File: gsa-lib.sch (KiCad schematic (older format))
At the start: 56 parts

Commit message: Update to support KiCad v5
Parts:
- BR?: symbol BRIDGE -> gsa:BRIDGE
- C?: symbol CAP -> gsa:CAP
- C?: symbol CAP-P -> gsa:CAP-P
- D?: symbol DIODE -> gsa:DIODE
- F?: symbol FUSE -> gsa:FUSE
- GND?: symbol EARTH -> gsa:EARTH
- GND?: symbol GND -> gsa:GND
- H?: symbol HOLE -> gsa:HOLE
- J?: symbol CONN-1 -> gsa:CONN-1
- J?: symbol CONN-2 -> gsa:CONN-2
- J?: symbol CONN-3 -> gsa:CONN-3
- J?: symbol CONN-4 -> gsa:CONN-4
- J?: symbol CONN-5 -> gsa:CONN-5
- LED: symbol LED -> gsa:LED
- Q?: symbol N-JFET -> gsa:N-JFET
- Q?: symbol NMOS-D -> gsa:NMOS-D
- Q?: symbol NMOS-E -> gsa:NMOS-E
- Q?: symbol NPN -> gsa:NPN
- Q?: symbol P-JFET -> gsa:P-JFET
- Q?: symbol PMOS-D -> gsa:PMOS-D
- Q?: symbol PMOS-E -> gsa:PMOS-E
- Q?: symbol PNP -> gsa:PNP
- R?: symbol RES -> gsa:RES
- R?: symbol REZ -> gsa:REZ
- RL?: symbol RELAY-DPDT -> gsa:RELAY-DPDT
- RL?: symbol RELAY-SPDT -> gsa:RELAY-SPDT
- SW?: symbol DPDT -> gsa:DPDT
- SW?: symbol SP-PUSH -> gsa:SP-PUSH
- SW?: symbol SP2T -> gsa:SP2T
- SW?: symbol SP3T -> gsa:SP3T
- SW?: symbol SPDT -> gsa:SPDT
- SW?: symbol SPST -> gsa:SPST
- SW?: symbol DPST -> gsa:DPST
- TX?: symbol XFRMR -> gsa:XFRMR
- TX?: symbol XFRMR-C -> gsa:XFRMR-C
- TX?: symbol XFRMR-D -> gsa:XFRMR-D
- U?: symbol 4017 -> gsa:4017
- U?: symbol 4066 -> gsa:4066
- U?: symbol 741 -> gsa:741
- U?: symbol LM1875 -> gsa:LM1875
- U?: symbol LM1876 -> gsa:LM1876
- U?: symbol LM317 -> gsa:LM317
- U?: symbol LM386 -> gsa:LM386
- U?: symbol LM377 -> gsa:LM377
- U?: symbol LM78XX -> gsa:LM78XX
- U?: symbol LM79XX -> gsa:LM79XX
- U?: symbol NE555 -> gsa:NE555
- U?: symbol OPAMP -> gsa:OPAMP
- U?: symbol TDA2009 -> gsa:TDA2009
- U?: symbol 40106 -> gsa:40106
- U?: symbol 4093 -> gsa:4093
- V?: symbol POWER -> gsa:POWER
- VR?: symbol POT -> gsa:POT
- VR?: symbol VR -> gsa:VR
- X?: symbol LINK -> gsa:LINK
- ZD?: symbol ZENER -> gsa:ZENER
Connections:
- net V+: no longer names the net of V?.1 (V+)
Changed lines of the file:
@@
-EESchema Schematic File Version 2
-LIBS:gsa
-EELAYER 25 0
+EESchema Schematic File Version 4
+LIBS:gsa-lib-cache
+EELAYER 29 0
 EELAYER END
 $Descr A4 11693 8268
@@
 Sheet 1 1
 Title "GSA Schematic Library"
-Date "January 2018"
-Rev "1.0.0"
+Date "January 2019"
+Rev "1.0.1"
 Comp "Gemstone Amplification"
-Comment1 "© Tim Baldwin 2016,2018"
+Comment1 "© Tim Baldwin 2016,2019"
 Comment2 ""
 Comment3 ""
@@
 $EndDescr
 $Comp
-L 4017 U?
+L gsa:4017 U?
 U 1 1 5A8F3386
 P 6700 1650
@@
 $EndComp
 $Comp
-L 4066 U?
+L gsa:4066 U?
 U 1 1 5A8F340F
 P 7350 1650
@@
 $EndComp
 $Comp
-L 741 U?
+L gsa:741 U?
 U 1 1 5A8F34D3
 P 8750 2000
@@
 $EndComp
 $Comp
-L CAP C?
+L gsa:CAP C?
 U 1 1 5A8F35EB
 P 2300 1850
@@
 $EndComp
 $Comp
-L CAP-P C?
+L gsa:CAP-P C?
 U 1 1 5A8F364A
 P 2650 1850
@@
 $EndComp
 $Comp
-L CONN-1 J?
+L gsa:CONN-1 J?
 U 1 1 5A8F36D3
 P 4200 1000
@@
 $EndComp
 $Comp
-L CONN-2 J?
+L gsa:CONN-2 J?
 U 1 1 5A8F3784
 P 4800 1000
@@
 $EndComp
 $Comp
-L CONN-3 J?
+L gsa:CONN-3 J?
 U 1 1 5A8F3805
 P 4200 1650
@@
 $EndComp
 $Comp
-L CONN-4 J?
+L gsa:CONN-4 J?
 U 1 1 5A8F3858
 P 4800 1550
@@
 $EndComp
 $Comp
-L CONN-5 J?
+L gsa:CONN-5 J?
 U 1 1 5A8F38D9
 P 5400 1500
@@
 $EndComp
 $Comp
-L DIODE D?
+L gsa:DIODE D?
 U 1 1 5A8F3942
 P 900 2700
@@
 $EndComp
 $Comp
-L DPDT SW?
+L gsa:DPDT SW?
 U 1 1 5A8F39ED
 P 2650 5500
@@
 $EndComp
 $Comp
-L EARTH GND?
+L gsa:EARTH GND?
 U 1 1 5A8F3BDA
 P 850 900
@@
 $EndComp
 $Comp
-L FUSE F?
+L gsa:FUSE F?
 U 1 1 5A8F3C0E
 P 2450 1100
@@
 $EndComp
 $Comp
-L GND GND?
+L gsa:GND GND?
 U 1 1 5A8F3CA5
 P 1250 900
@@
 $EndComp
 $Comp
-L HOLE H?
+L gsa:HOLE H?
 U 1 1 5A8F3CDB
 P 3300 1000
@@
 $EndComp
 $Comp
-L LED LED
+L gsa:LED LED
 U 1 1 5A8F3D22
 P 1900 2700
@@
 $EndComp
 $Comp
-L LINK X?
+L gsa:LINK X?
 U 1 1 5A8F3DA3
 P 750 1850
@@
 $EndComp
 $Comp
-L LM1875 U?
+L gsa:LM1875 U?
 U 1 1 5A8F3E65
 P 6950 5850
@@
 $EndComp
 $Comp
-L LM1876 U?
+L gsa:LM1876 U?
 U 1 1 5A8F3F6A
 P 8200 5300
@@
 $EndComp
 $Comp
-L LM317 U?
+L gsa:LM317 U?
 U 1 1 5A8F400B
 P 7700 2900
@@
 $EndComp
 $Comp
-L LM386 U?
+L gsa:LM386 U?
 U 1 1 5A8F40AC
 P 6950 4750
@@
 $EndComp
 $Comp
-L LM377 U?
+L gsa:LM377 U?
 U 1 1 5A8F4141
 P 7700 3500
@@
 $EndComp
 $Comp
-L LM78XX U?
+L gsa:LM78XX U?
 U 1 1 5A8F4204
 P 6850 2900
@@
 $EndComp
 $Comp
-L LM79XX U?
+L gsa:LM79XX U?
 U 1 1 5A8F42A3
 P 6850 3500
@@
 $EndComp
 $Comp
-L N-JFET Q?
+L gsa:N-JFET Q?
 U 1 1 5A8F4376
 P 1550 3500
@@
 $EndComp
 $Comp
-L NE555 U?
+L gsa:NE555 U?
 U 1 1 5A8F43F7
 P 10300 1200
@@
 $EndComp
 $Comp
-L NMOS-D Q?
+L gsa:NMOS-D Q?
 U 1 1 5A8F44CE
 P 2250 3500
@@
 $EndComp
 $Comp
-L NMOS-E Q?
+L gsa:NMOS-E Q?
 U 1 1 5A8F4559
 P 3000 3500
@@
 $EndComp
 $Comp
-L NPN Q?
+L gsa:NPN Q?
 U 1 1 5A8F4612
 P 950 3500
@@
 $EndComp
 $Comp
-L OPAMP U?
+L gsa:OPAMP U?
 U 1 1 5A8F46A9
 P 8750 1200
@@
 $EndComp
 $Comp
-L P-JFET Q?
+L gsa:P-JFET Q?
 U 1 1 5A8F48D1
 P 1550 4000
@@
 $EndComp
 $Comp
-L PMOS-D Q?
+L gsa:PMOS-D Q?
 U 1 1 5A8F49FE
 P 2250 4000
@@
 $EndComp
 $Comp
-L PMOS-E Q?
+L gsa:PMOS-E Q?
 U 1 1 5A8F4BA5
 P 3000 4000
@@
 $EndComp
 $Comp
-L PNP Q?
+L gsa:PNP Q?
 U 1 1 5A8F4C98
 P 950 4000
@@
 $EndComp
 $Comp
-L POT VR?
+L gsa:POT VR?
 U 1 1 5A8F4D9A
 P 1900 1850
@@
 $EndComp
 $Comp
-L POWER V?
+L gsa:POWER V?
 U 1 1 5A8F5493
 P 1600 1200
@@
 $EndComp
 $Comp
-L PWR_FLAG #FLG?
+L gsa:PWR_FLAG #FLG?
 U 1 1 5A8F56BB
 P 2000 1150
@@
 $EndComp
 $Comp
-L RELAY-DPDT RL?
+L gsa:RELAY-DPDT RL?
 U 1 1 5A8F57B3
 P 2000 6700
@@
 $EndComp
 $Comp
-L RELAY-SPDT RL?
+L gsa:RELAY-SPDT RL?
 U 1 1 5A8F5882
 P 1100 6700
@@
 $EndComp
 $Comp
-L RES R?
+L gsa:RES R?
 U 1 1 5A8F5927
 P 1000 1850
@@
 $EndComp
 $Comp
-L REZ R?
+L gsa:REZ R?
 U 1 1 5A8F5B46
 P 1300 1850
@@
 $EndComp
 $Comp
-L SP-PUSH SW?
+L gsa:SP-PUSH SW?
 U 1 1 5A8F5BF7
 P 1100 4800
@@
 $EndComp
 $Comp
-L SP2T SW?
+L gsa:SP2T SW?
 U 1 1 5A8F5CB0
 P 3450 4800
@@
 $EndComp
 $Comp
-L SP3T SW?
+L gsa:SP3T SW?
 U 1 1 5A8F5D5D
 P 3450 5450
@@
 $EndComp
 $Comp
-L SPDT SW?
+L gsa:SPDT SW?
 U 1 1 5A8F6176
 P 2650 4800
@@
 $EndComp
 $Comp
-L SPST SW?
+L gsa:SPST SW?
 U 1 1 5A8F620B
 P 1850 4800
@@
 $EndComp
 $Comp
-L TDA2009 U?
+L gsa:TDA2009 U?
 U 1 1 5A8F62FA
 P 9550 5350
@@
 $EndComp
 $Comp
-L VR VR?
+L gsa:VR VR?
 U 1 1 5A8F63A9
 P 1600 1850
@@
 $EndComp
 $Comp
-L XFRMR TX?
+L gsa:XFRMR TX?
 U 1 1 5A8F64C2
 P 4050 6900
@@
 $EndComp
 $Comp
-L XFRMR-C TX?
+L gsa:XFRMR-C TX?
 U 1 1 5A8F6591
 P 4950 6900
@@
 $EndComp
 $Comp
-L XFRMR-D TX?
+L gsa:XFRMR-D TX?
 U 1 1 5A8F6658
 P 5800 6900
@@
 $EndComp
 $Comp
-L ZENER ZD?
+L gsa:ZENER ZD?
 U 1 1 5A8F6725
 P 1400 2700
@@
 Passives
 $Comp
-L BRIDGE BR?
+L gsa:BRIDGE BR?
 U 1 1 5A8FA025
 P 2600 2700
@@
 Op Amps
 $Comp
-L 40106 U?
+L gsa:40106 U?
 U 1 1 5A8FFB7C
 P 6600 950
@@
 $EndComp
 $Comp
-L 4093 U?
+L gsa:4093 U?
 U 1 1 5A8FFBC9
 P 7150 950
@@
 Voltage Regulators
 $Comp
-L DPST SW?
+L gsa:DPST SW?
 U 1 1 5A9011BD
 P 1850 5500

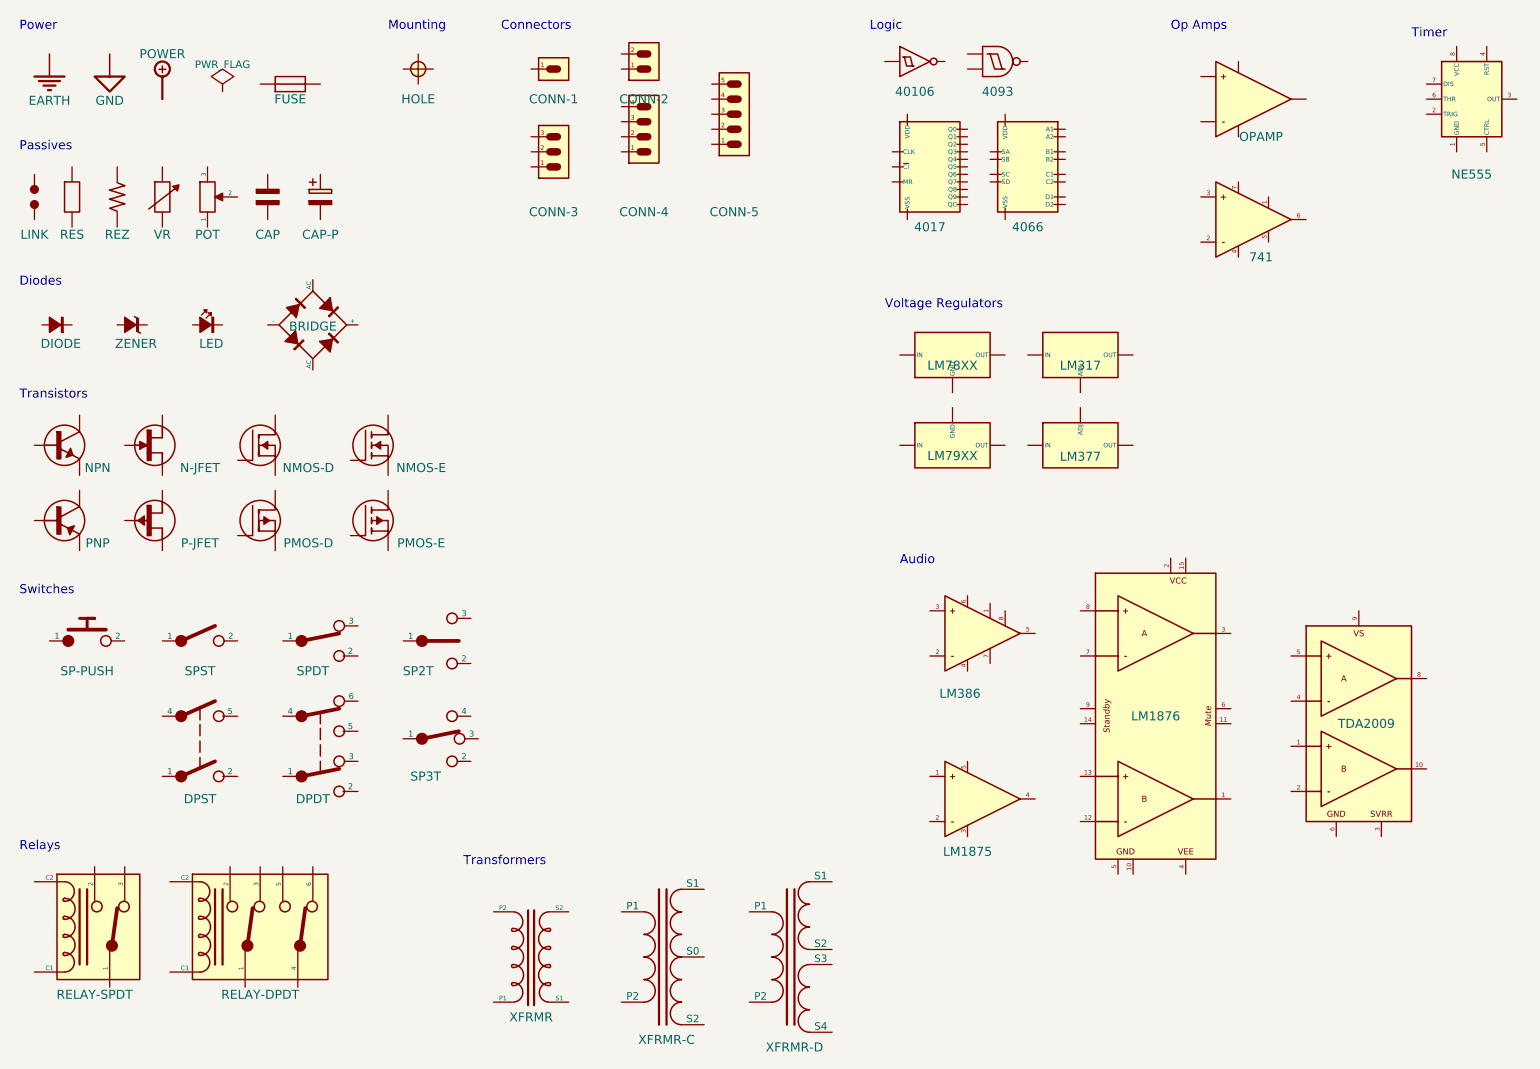
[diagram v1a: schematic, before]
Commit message: Symbol and Footprint updates for GSA Emerald II
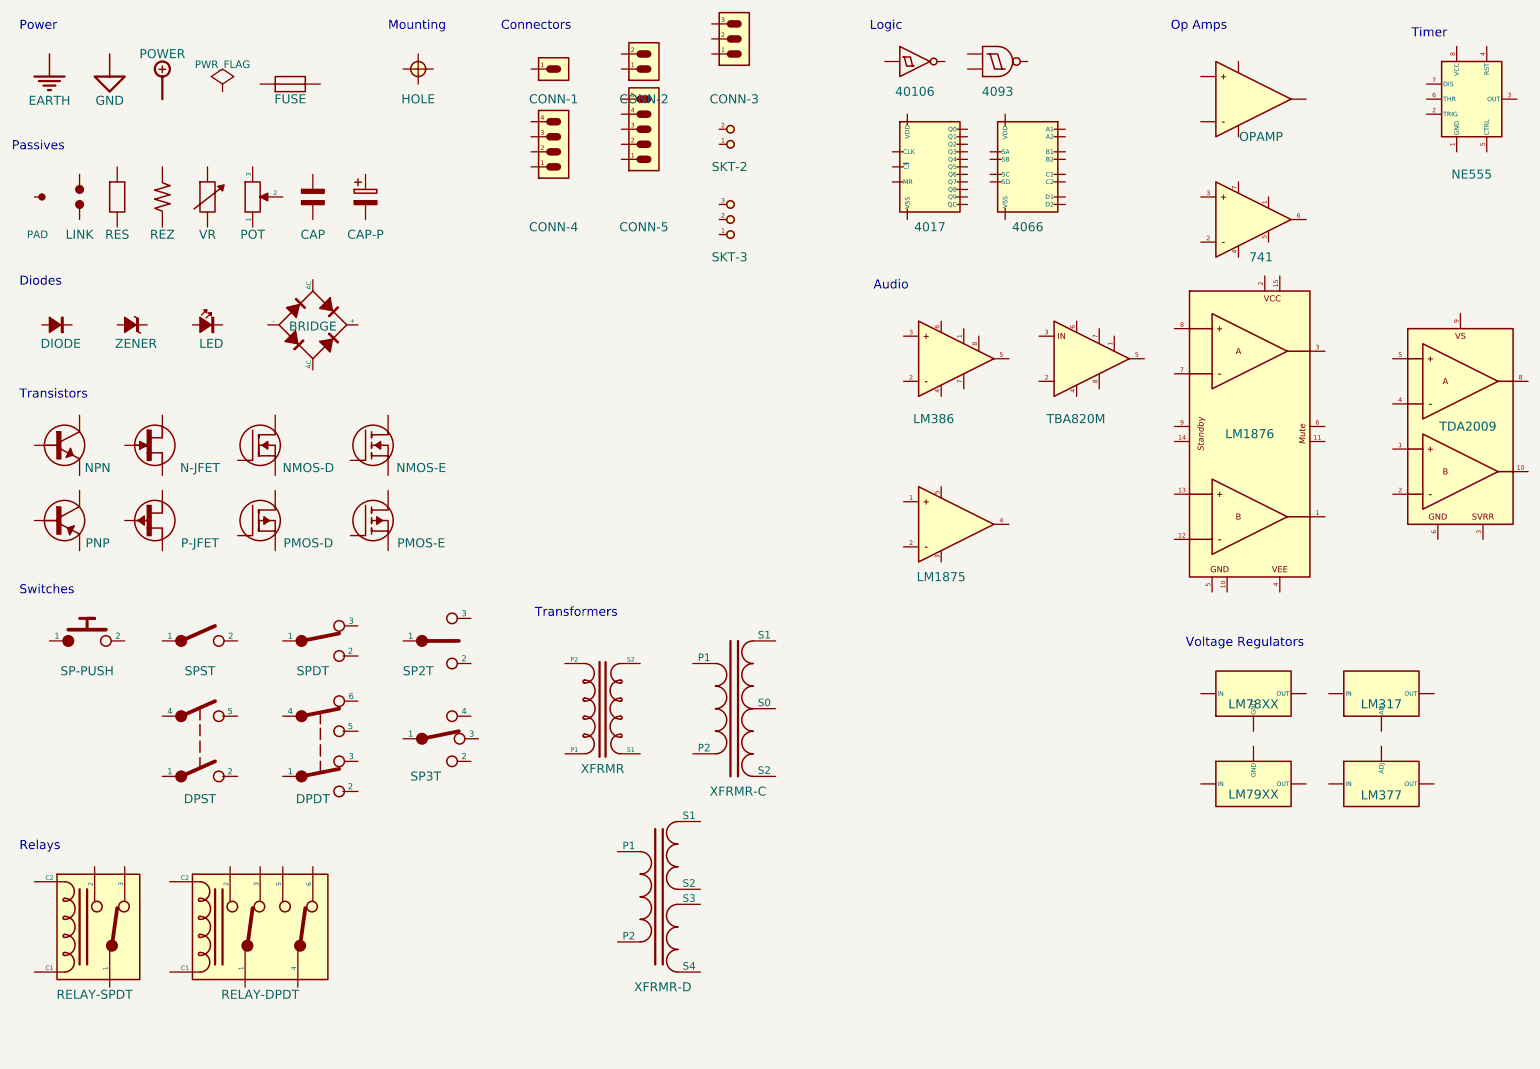
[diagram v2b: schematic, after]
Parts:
- added J?: SKT-2, symbol gsa:SKT-2
- added J?: SKT-3, symbol gsa:SKT-3
- added JP?: PAD, symbol gsa:PAD
- added U?: TBA820M, symbol gsa:TBA820M

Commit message: Overhaul and tidy-up of symbols, footprints and 3D models
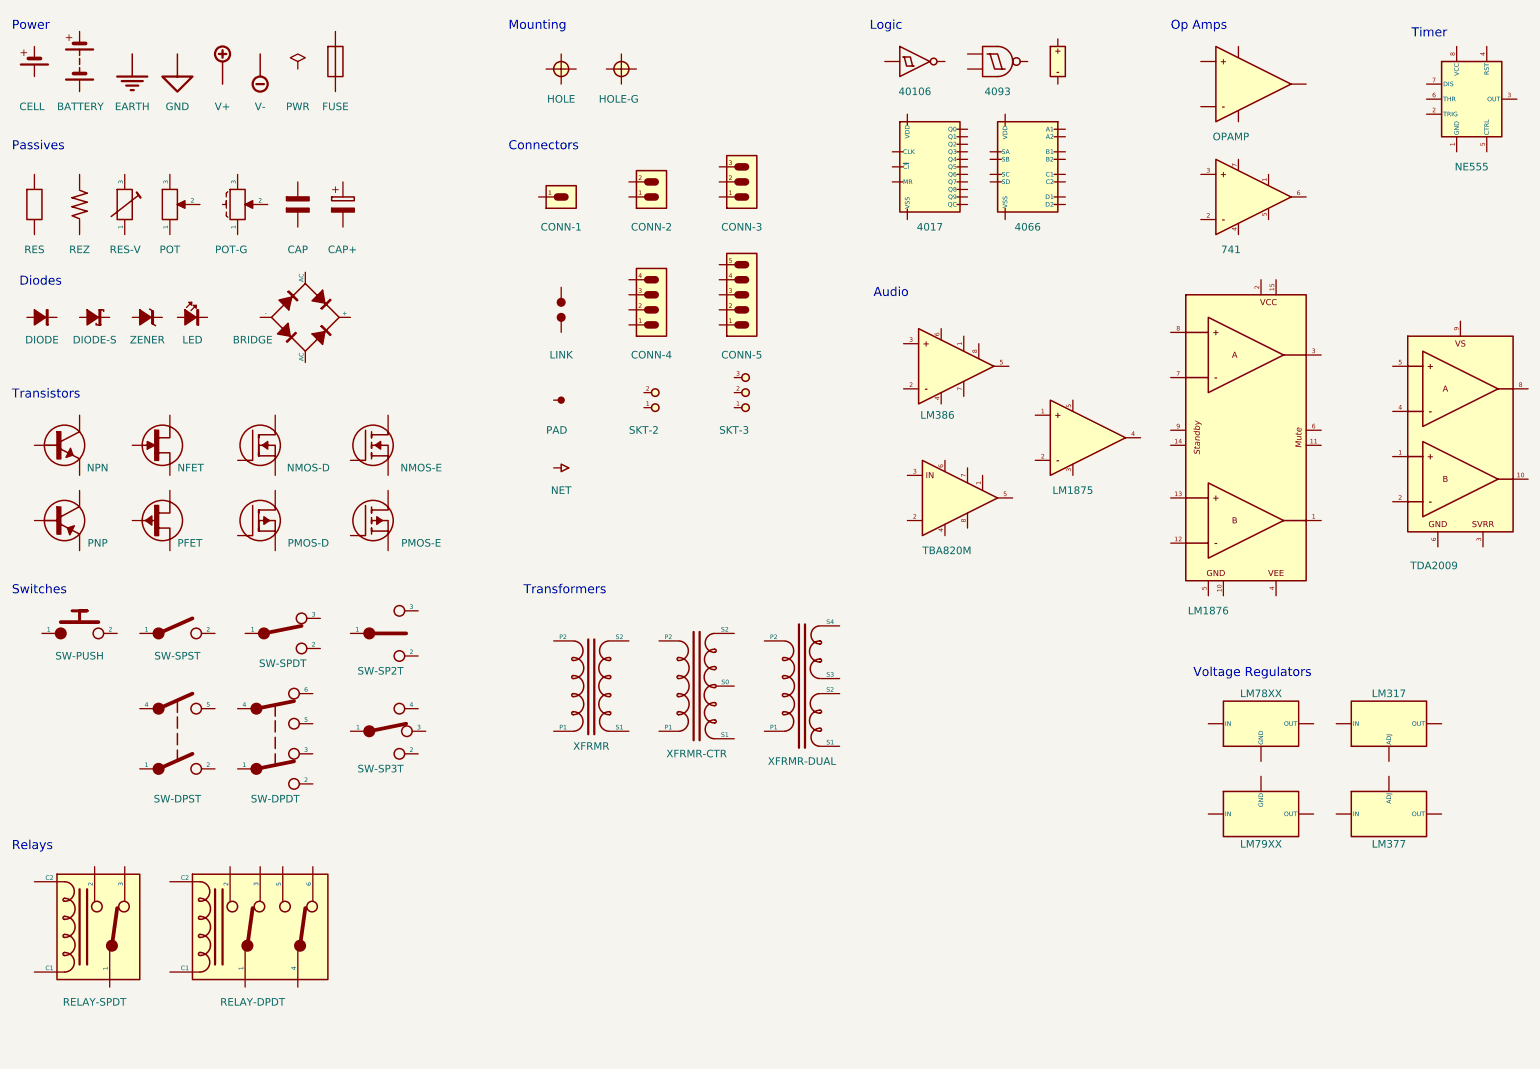
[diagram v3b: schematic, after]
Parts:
- removed C?: CAP-P, symbol gsa:CAP-P
- removed GND?: EARTH, symbol gsa:EARTH
- removed GND?: GND, symbol gsa:GND
- removed JP?: PAD, symbol gsa:PAD
- removed Q?: N-JFET, symbol gsa:N-JFET
- removed Q?: P-JFET, symbol gsa:P-JFET
- removed SW?: DPDT, symbol gsa:DPDT
- removed SW?: SP-PUSH, symbol gsa:SP-PUSH
- removed SW?: SP2T, symbol gsa:SP2T
- removed SW?: SP3T, symbol gsa:SP3T
- removed SW?: SPDT, symbol gsa:SPDT
- removed SW?: SPST, symbol gsa:SPST
- removed SW?: DPST, symbol gsa:DPST
- removed TX?: XFRMR-C, symbol gsa:XFRMR-C
- removed TX?: XFRMR-D, symbol gsa:XFRMR-D
- removed V?: POWER, symbol gsa:POWER
- removed VR?: VR, symbol gsa:VR
- removed ZD?: ZENER, symbol gsa:ZENER
- added C2: CAP+, symbol gsa:CAP+
- added D?: DIODE-S, symbol gsa:DIODE-S
- added H2: HOLE-G, symbol gsa:HOLE-G
- added JP1: PAD, symbol gsa:PAD
- added Q3: NFET, symbol gsa:NFET
- added Q4: PFET, symbol gsa:PFET
- added SW1: SW-PUSH, symbol gsa:SW-PUSH
- added SW2: SW-SPST, symbol gsa:SW-SPST
- added SW3: SW-DPST, symbol gsa:SW-DPST
- added SW4: SW-DPDT, symbol gsa:SW-DPDT
- added SW5: SW-SPDT, symbol gsa:SW-SPDT
- added SW6: SW-SP2T, symbol gsa:SW-SP2T
- added SW7: SW-SP3T, symbol gsa:SW-SP3T
- added T2: XFRMR-CTR, symbol gsa:XFRMR-CTR
- added T3: XFRMR-DUAL, symbol gsa:XFRMR-DUAL
- added unit 7 of U1
- added VR1: RES-V, symbol gsa:RES-V
- added VR3: POT-G, symbol gsa:POT-G
- added Z?: ZENER, symbol gsa:ZENER
- gave numbers to parts that had none: 41
- renumbered LED to LED1
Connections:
- net GND: now also H2.0 (GND), VR3.0 (GND)
- new net: VR1.1, VR1.2 (1)
